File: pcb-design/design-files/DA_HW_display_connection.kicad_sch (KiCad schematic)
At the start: 51 parts, among them J3 62684-502100ALF, Q1 1AM, U4 TPS61165DBV, U5 TPS61040DBV

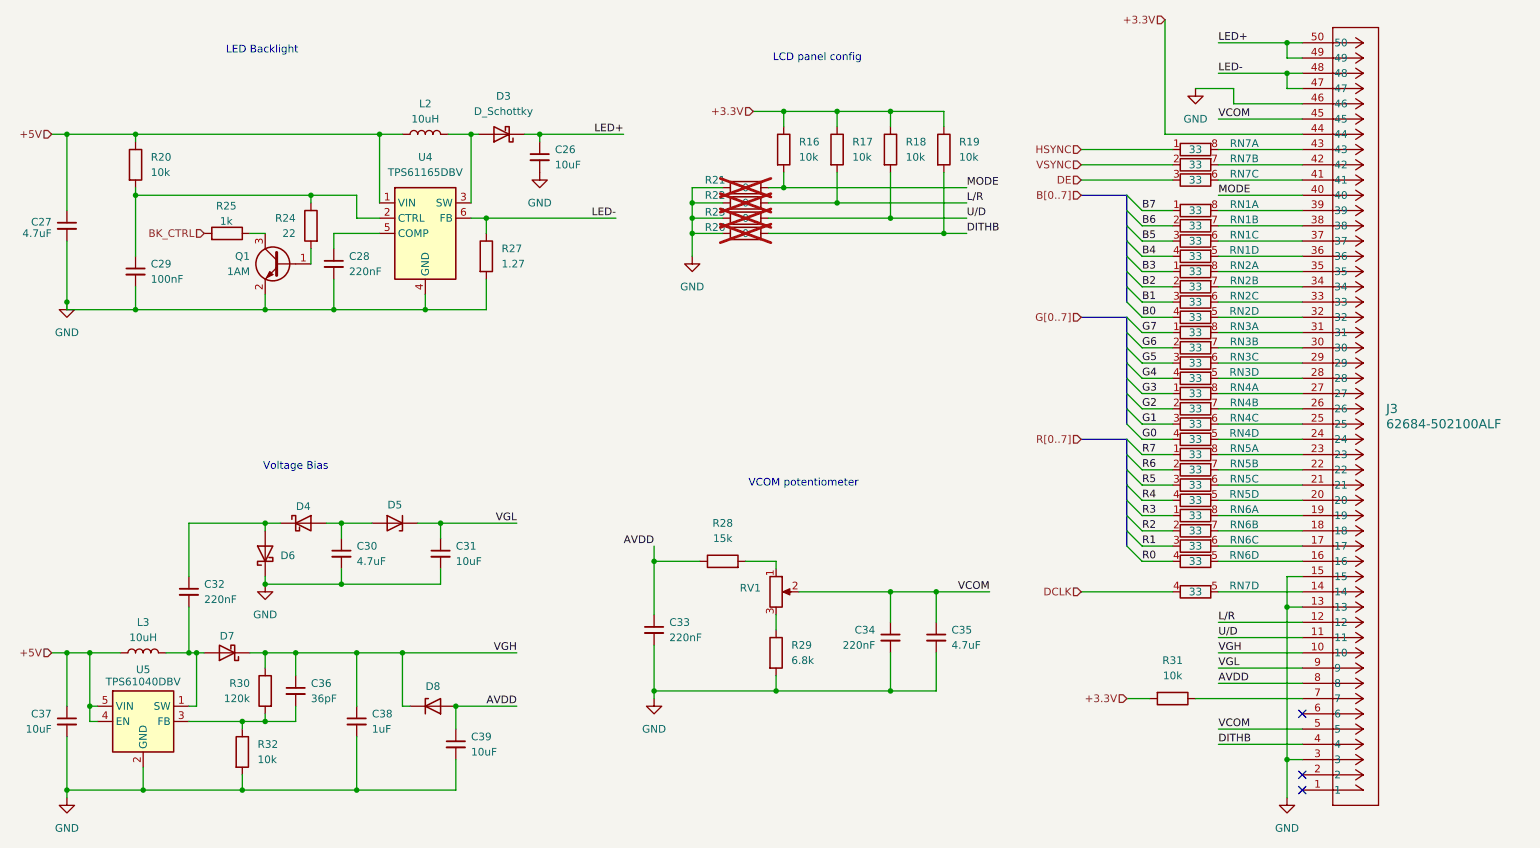
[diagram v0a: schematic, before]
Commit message: Fix HW rev B issues
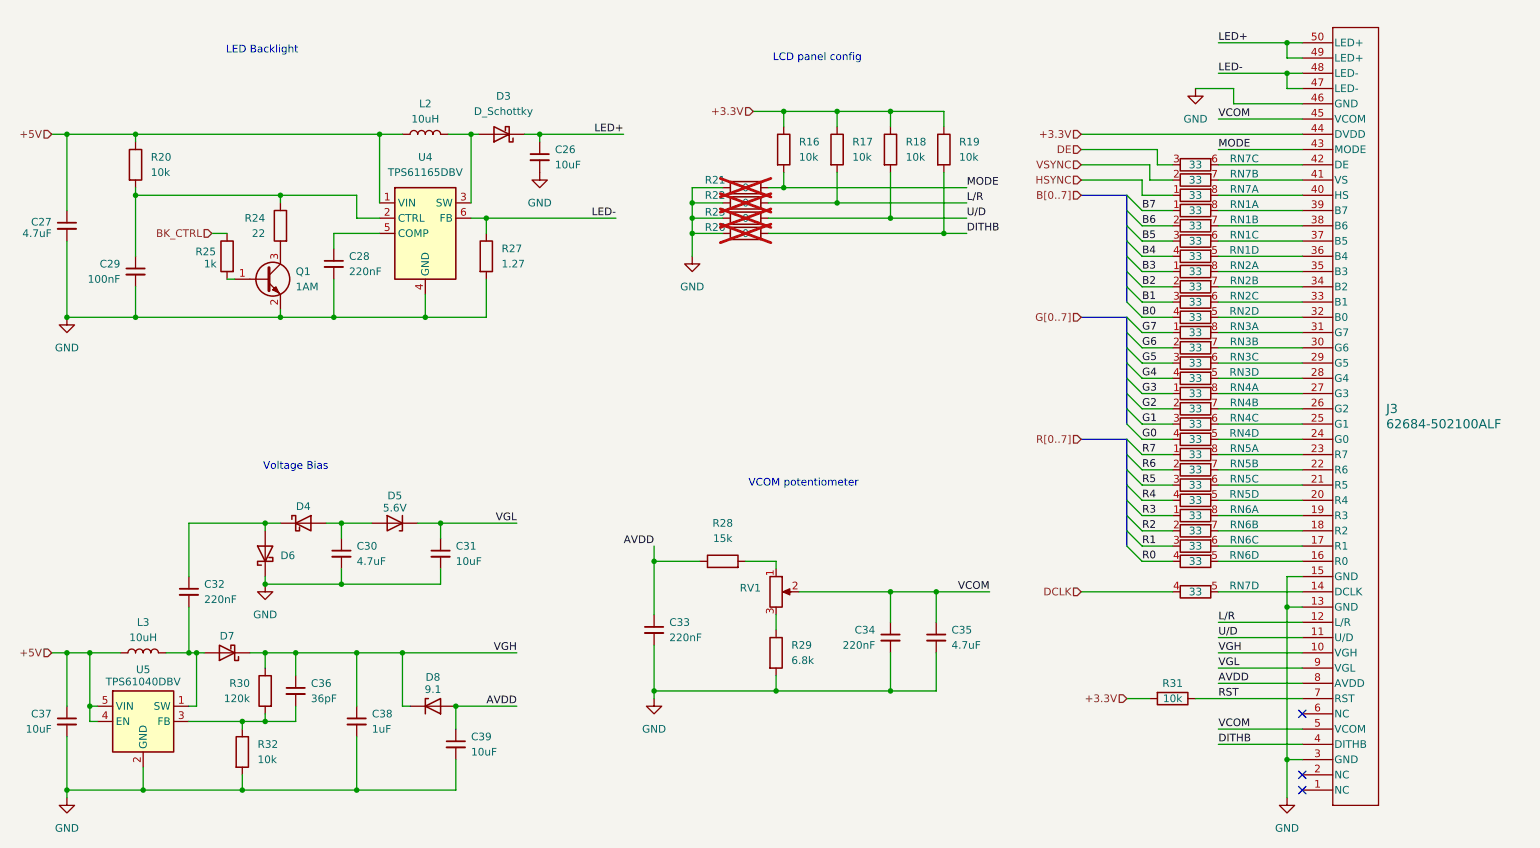
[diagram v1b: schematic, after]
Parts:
- D5: value D_Zener -> 5.6V
- D8: value D_Zener -> 9.1
- J3: footprint Deskassistant_HW:CONN_AMPHENOL_62684-502100ALF -> Deskassistant_HW:CONN50_62684-502100ALF_FCI
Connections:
- net BK_CTRL: now also R25.1; no longer R25.2
- net MODE: now also J3.43 (MODE); no longer J3.40
- net at RN7.8 (R1.2): now also J3.40 (HS); no longer J3.43
- net at J3.41 (VS): now also RN7.7 (R2.2); no longer RN7.6 (R3.2)
- net at J3.42 (DE): now also RN7.6 (R3.2); no longer RN7.7 (R2.2)
- net RST: now reaches J3.7 (RST), R31.1
- net at Q1.3 (C): now also R24.2; no longer R25.1
- net at Q1.1 (B): now also R25.2; no longer R24.2
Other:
- moved on the sheet: Q1, R24, R25, RN7A, RN7B, RN7C

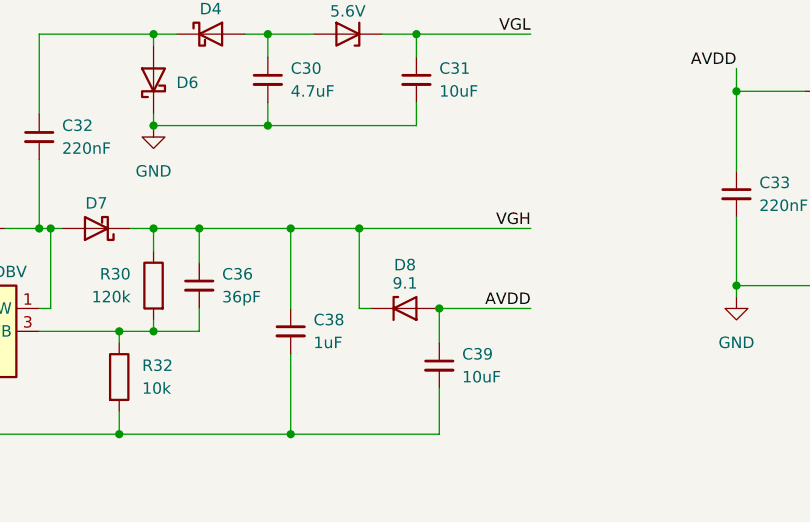
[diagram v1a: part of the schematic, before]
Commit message: Add unit of measure to D8 value
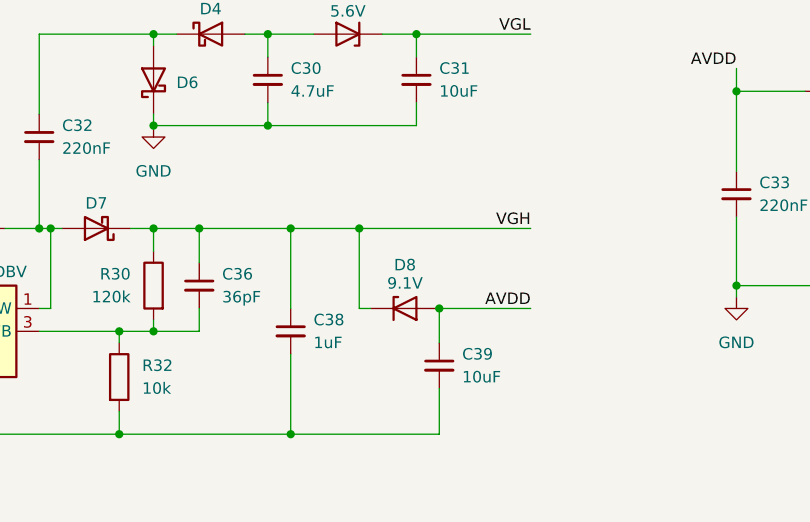
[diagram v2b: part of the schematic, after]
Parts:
- D8: value 9.1 -> 9.1V
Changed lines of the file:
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@@
 			)
 		)
-		(property "Value" "9.1"
+		(property "Value" "9.1V"
 			(at 96.52 138.176 0)
 			(effects
